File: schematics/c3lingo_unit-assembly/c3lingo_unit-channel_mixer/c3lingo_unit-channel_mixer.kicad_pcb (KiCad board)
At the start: 2 copper layers, 75 x 183 mm, 120 parts, among them J301 Mic X In, J302 Headphone X, J303 PowerSupply, J304 Inputs, J305 Output, J306 PowerSupply, J307 Interconnect, J308 Interconnect, SW301 OnAir_X, SW302 Mute_X, U301 NE5534, U302 LM833N, U303 LM386N-4, U304 LM833N, U305 LM339, U306 LM339, U307 LM339

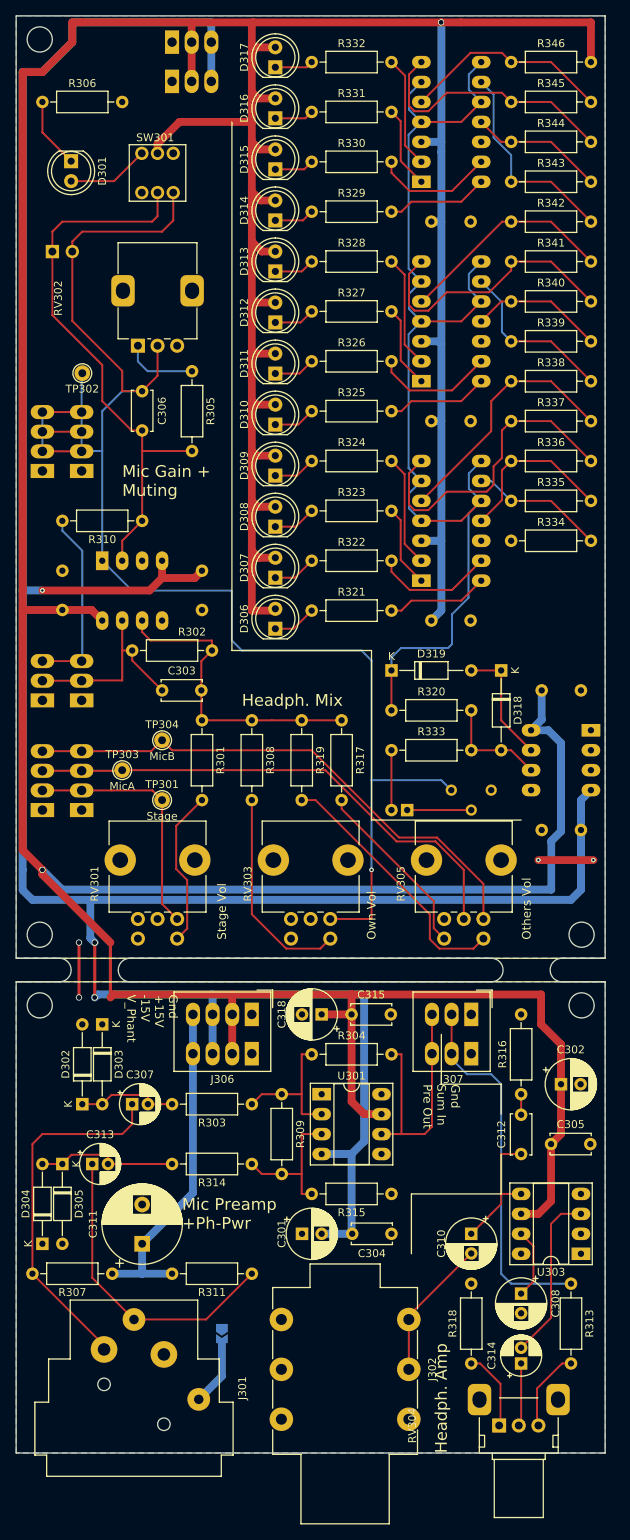
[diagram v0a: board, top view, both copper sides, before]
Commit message: [TIDY] Split channel into two schematics
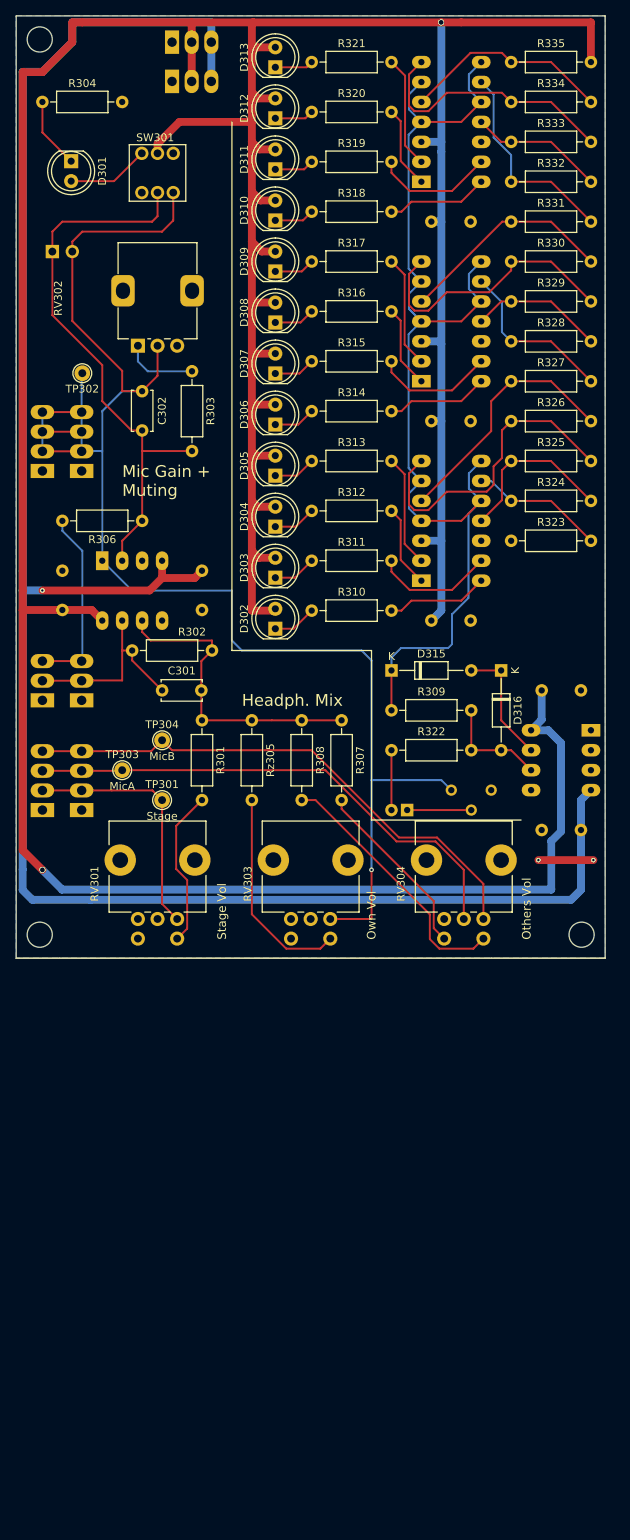
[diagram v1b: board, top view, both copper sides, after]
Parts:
- removed the C301 at (86.4, 205.1)
- removed the C302 at (119.4, 186.0)
- removed the C304 at (97.8, 205.1)
- removed the C305 at (118.1, 193.7)
- removed the C307 at (64.8, 188.6)
- removed the C308 at (114.3, 212.7)
- removed the C310 at (108.0, 205.1)
- removed C311: 100uF/ 63V, Capacitor_THT:CP_Radial_D10.0mm_P5.00mm
- removed C312: 47nF, Capacitor_THT:C_Disc_D5.0mm_W2.5mm_P5.00mm
- removed C313: 1uF/ 63V lowESR, Capacitor_THT:CP_Radial_D5.0mm_P2.00mm
- removed C314: 1uF, Capacitor_THT:CP_Radial_D5.0mm_P2.00mm
- removed C315: 100nF, Capacitor_THT:C_Disc_D5.0mm_W2.5mm_P5.00mm
- removed C318: 100uF, Capacitor_THT:CP_Radial_D6.3mm_P2.50mm
- removed the D302 at (58.4, 188.6)
- removed the D303 at (61.0, 178.4)
- removed the D304 at (53.3, 206.4)
- removed the D305 at (55.9, 196.2)
- removed H305, H306: MountingHole, MountingHole:MountingHole_3.2mm_M3
- removed the J302 at (100.0, 216.0)
- removed J306: PowerSupply, TerminalBlock_Phoenix:TerminalBlock_Phoenix_PTSM-0,5-4-2.5-H-THR_1x04_P2.50mm_Horizontal
- removed J307, J308: Interconnect, TerminalBlock_Phoenix:TerminalBlock_Phoenix_PTSM-0,5-3-2.5-H-THR_1x03_P2.50mm_Horizontal
- removed JP302: GND_JMP, Jumper:SolderJumper-2_P1.3mm_Open_TrianglePad1.0x1.5mm
- removed the R303 at (80.0, 188.6)
- removed the R304 at (87.6, 182.2)
- removed the R307 at (62.2, 210.2)
- removed the R308 at (80.0, 139.7)
- removed the R309 at (83.8, 187.3)
- removed the R310 at (66.0, 114.3)
- removed the R311 at (80.0, 210.2)
- removed the R313 at (120.7, 211.4)
- removed the R314 at (80.0, 196.2)
- removed the R315 at (97.8, 200.0)
- removed the R316 at (114.3, 187.3)
- removed the R318 at (108.0, 221.6)
- removed the RV304 at (111.5, 229.5)
- removed the U301 at (88.9, 187.3)
- removed the U303 at (121.9, 207.6)
- added R306: 330R, Resistor_THT:R_Axial_DIN0207_L6.3mm_D2.5mm_P10.16mm_Horizontal, F.Cu at (66.0, 114.3)
- added Rz305: 22K, Resistor_THT:R_Axial_DIN0207_L6.3mm_D2.5mm_P10.16mm_Horizontal, F.Cu at (80.0, 139.7)
- J301: value Mic X In -> Interconnect; footprint Connector_Audio:Jack_XLR_Neutrik_NC3FAAH2_Horizontal -> TerminalBlock_Phoenix:TerminalBlock_Phoenix_PTSM-0,5-3-2.5-H-THR_1x03_P2.50mm_Horizontal; moved to B.Cu
- moved J301 84.7 mm to (53.3, 137.2), turned to 90 degrees
- renumbered C303 to C301, C306 to C302, C316 to C303, C317 to C304, C319 to C305, C321 to C306, C322 to C307, C323 to C308, C324 to C309, C325 to C310, D306 to D302, D307 to D303, D308 to D304, D309 to D305, D310 to D306, D311 to D307, D312 to D308, D313 to D309, D314 to D310, D315 to D311, D316 to D312, D317 to D313, D319 to D315, D318 to D316, J303 to J302, J305 to J303, R305 to R303, R306 to R304, R317 to R307, R319 to R308, R320 to R309, R321 to R310, R322 to R311, R323 to R312, R324 to R313, R325 to R314, R326 to R315, R327 to R316, R328 to R317, R329 to R318, R330 to R319, R331 to R320, R332 to R321, R333 to R322, R334 to R323, R335 to R324, R336 to R325, R337 to R326, R338 to R327, R339 to R328, R340 to R329, R341 to R330, R342 to R331, R343 to R332, R344 to R333, R345 to R334, R346 to R335, RV305 to RV304, RV306 to RV305, U302 to U301, U305 to U302, U306 to U303, U307 to U304, U304 to U305
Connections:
- C301 pad 1: SumOut -> /HeadphoneMix
- J301 pad 2: Net-(C307-Pad1) -> /HeadphoneMix
- J301 pad 3: Net-(C313-Pad1) -> /MicGainIn
- R302 pad 1: SumOut -> /HeadphoneMix
- U301 pad 7: SumOut -> /HeadphoneMix
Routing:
- net +15V: track 649.8 -> 513.1 mm
- net -15V: track 344.7 -> 251.3 mm, vias 3 -> 1
- net AmpIn: track 46.9 -> 0.00 mm
- net Net-(C307-Pad1): track 46.2 -> 0.00 mm
- net V_Phant: track 43.3 -> 0.00 mm
- net Net-(C313-Pad1): track 39.4 -> 0.00 mm
- net MicPreOut: track 32.7 -> 0.00 mm
- net SumOut: track 25.7 -> 0.00 mm
- net /HeadphoneMix: track 0.00 -> 25.7 mm
- net MicGainIn: track 23.8 -> 0.00 mm
- net /MicGainIn: track 0.00 -> 23.8 mm
- net Net-(C314-Pad2): track 21.7 -> 0.00 mm
- net Net-(R309-Pad2): track 18.3 -> 0.00 mm
- net Net-(R303-Pad1) (its old number): track 18.3 -> 0.00 mm
- net Net-(C313-Pad2): track 18.1 -> 0.00 mm
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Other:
- board size 75 x 183 mm -> 75 x 120 mm
- board text removed: "Gnd +15V -15V V_Phant"
- board text removed: "Gnd Sum In Pre Out"
- board text removed: "Headph. Amp"
- board text removed: "Mic Preamp +Ph-Pwr"
- board text removed: "c3lingo Interpreter Unit v0.3 2023-12-30 Jannik Beyerstedt (jtbx)"

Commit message: Update to KiCad 7
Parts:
- removed D316: 1N4148, Diode_THT:D_DO-35_SOD27_P10.16mm_Horizontal
- removed Rz305: 22K, Resistor_THT:R_Axial_DIN0207_L6.3mm_D2.5mm_P10.16mm_Horizontal
- added D314: 1N4148, Diode_THT:D_DO-35_SOD27_P10.16mm_Horizontal, F.Cu at (111.8, 133.3)
- added R305: 22K, Resistor_THT:R_Axial_DIN0207_L6.3mm_D2.5mm_P10.16mm_Horizontal, F.Cu at (80.0, 139.7)
- C302: value 100nF -> 10nF

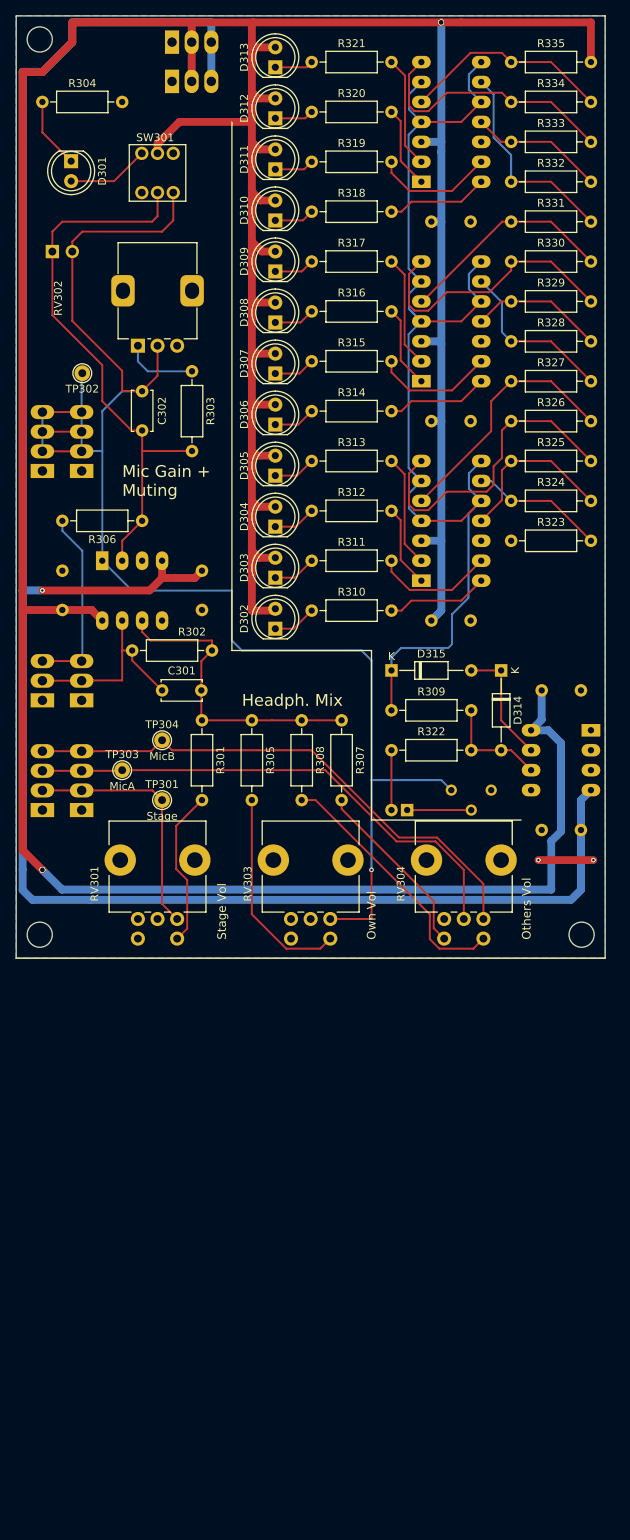
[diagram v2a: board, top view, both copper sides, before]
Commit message: Re-layout boards with SMD components
* Channel Mix: Removed vu meter potentiometer as good setting was found (10 dB
  more headroom)
* Channel Mix: Add vu meter alternate power
* Channel I/O: Added jumper for phantom power enable/disable
* Add GND test points
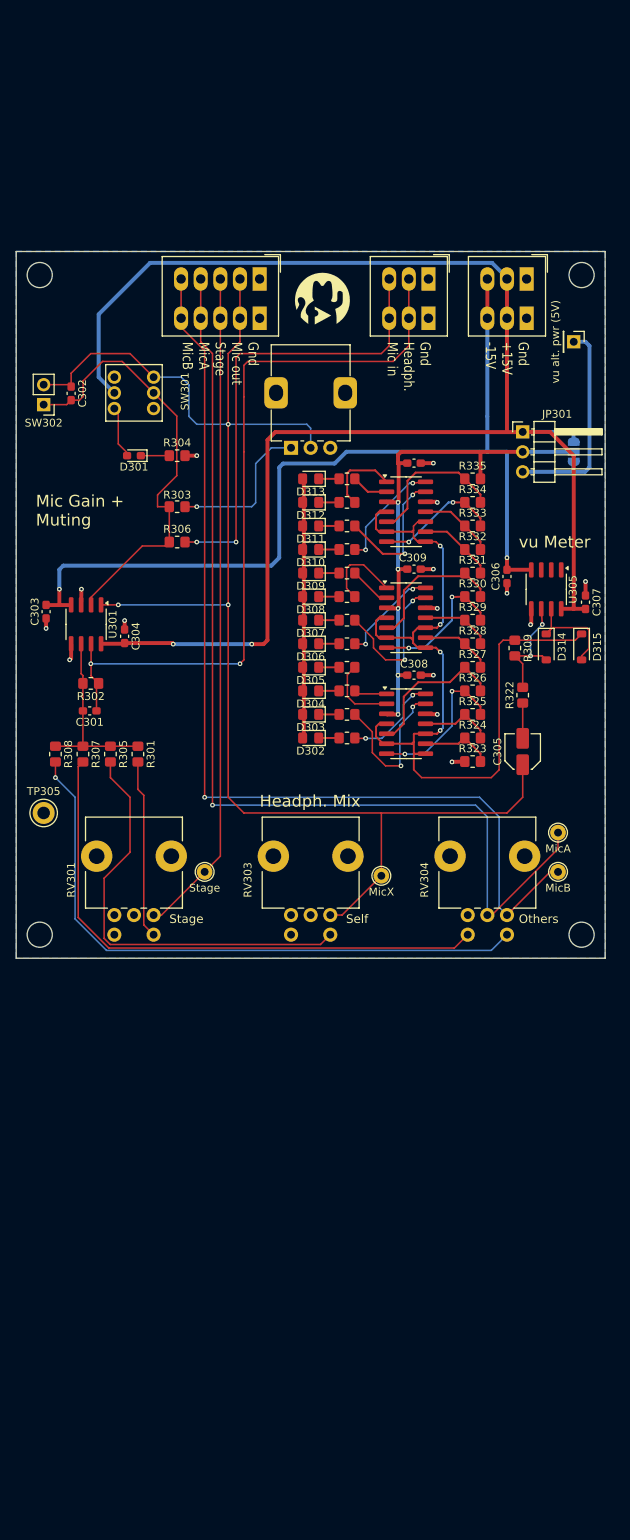
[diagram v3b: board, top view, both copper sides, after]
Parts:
- removed RV305: 50K, Potentiometer_THT:Potentiometer_Vishay_T73XX_Horizontal
- added G***: LOGO, c3lingo_unit-footprints:voctocat-07mm, F.Cu at (89.0, 86.0)
- added G***: LOGO, c3lingo_unit-footprints:voctocat-25mm, B.Cu at (87.5, 121.0)
- added H304: MountingHole, MountingHole:MountingHole_3.2mm_M3, F.Cu at (122.0, 83.0)
- added JP301: vu PWR, Connector_PinHeader_2.54mm:PinHeader_1x03_P2.54mm_Horizontal, F.Cu at (114.5, 103.0)
- added JP302: vu PWR, Jumper:SolderJumper-3_P1.3mm_Open_RoundedPad1.0x1.5mm_NumberLabels, B.Cu at (121.0, 105.5)
- added TP305: GND, TestPoint:TestPoint_Keystone_5005-5009_Compact, F.Cu at (53.5, 151.5)
- C301, C302: footprint Capacitor_THT:C_Disc_D5.0mm_W2.5mm_P5.00mm -> Capacitor_SMD:C_0603_1608Metric_Pad1.08x0.95mm_HandSolder
- C303, C304, C306, C307, C308, C309, C310: footprint Capacitor_THT:C_Disc_D5.0mm_W2.5mm_P5.00mm -> Capacitor_SMD:C_0603_1608Metric_Pad1.08x0.95mm_HandSolder; moved to F.Cu
- C305: footprint Capacitor_THT:CP_Radial_D5.0mm_P2.00mm -> Capacitor_SMD:C_Elec_4x5.8; moved to F.Cu
- D301: footprint LED_THT:LED_D5.0mm -> LED_SMD:LED_0603_1608Metric_Pad1.05x0.95mm_HandSolder
- D302, D303, D304, D305, D306, D307, D308, D309, D310, D311, D312, D313: footprint LED_THT:LED_D5.0mm -> LED_SMD:LED_0805_2012Metric_Pad1.15x1.40mm_HandSolder
- D314, D315: footprint Diode_THT:D_DO-35_SOD27_P10.16mm_Horizontal -> Diode_SMD:D_SOD-123
- J301, J302, SW302: moved to F.Cu
- J303: value Output -> I/O; footprint TerminalBlock_Phoenix:TerminalBlock_Phoenix_PTSM-0,5-4-2.5-H-THR_1x04_P2.50mm_Horizontal -> TerminalBlock_Phoenix:TerminalBlock_Phoenix_PTSM-0,5-5-2.5-H-THR_1x05_P2.50mm_Horizontal; moved to F.Cu
- J304: value Inputs -> vu alt. pwr (5V); footprint TerminalBlock_Phoenix:TerminalBlock_Phoenix_PTSM-0,5-4-2.5-H-THR_1x04_P2.50mm_Horizontal -> Connector_PinHeader_2.54mm:PinHeader_1x01_P2.54mm_Vertical; moved to F.Cu
- R301, R302, R303, R304, R305, R306, R307, R308, R322, R323, R324, R325, R326, R327, R328, R329, R330, R331, R332, R333, R334, R335: footprint Resistor_THT:R_Axial_DIN0207_L6.3mm_D2.5mm_P10.16mm_Horizontal -> Resistor_SMD:R_0805_2012Metric_Pad1.20x1.40mm_HandSolder
- R309: value 15K -> 12K; footprint Resistor_THT:R_Axial_DIN0207_L6.3mm_D2.5mm_P10.16mm_Horizontal -> Resistor_SMD:R_0805_2012Metric_Pad1.20x1.40mm_HandSolder
- R310, R311, R312, R313, R314, R315, R319, R320, R321: value 390R -> 680R; footprint Resistor_THT:R_Axial_DIN0207_L6.3mm_D2.5mm_P10.16mm_Horizontal -> Resistor_SMD:R_0805_2012Metric_Pad1.20x1.40mm_HandSolder
- R316, R317, R318: value 390R -> 620R; footprint Resistor_THT:R_Axial_DIN0207_L6.3mm_D2.5mm_P10.16mm_Horizontal -> Resistor_SMD:R_0805_2012Metric_Pad1.20x1.40mm_HandSolder
- U301, U305: value LM833N -> LM833-N; footprint Package_DIP:DIP-8_W7.62mm_Socket_LongPads -> Package_SO:SOIC-8_3.9x4.9mm_P1.27mm; moved to F.Cu
- U302, U303, U304: footprint Package_DIP:DIP-14_W7.62mm_Socket_LongPads -> Package_SO:SOIC-14_3.9x8.7mm_P1.27mm; moved to F.Cu
- moved J304 90.2 mm to (121.0, 91.5), turned to -90 degrees
- moved TP302 74.5 mm to (96.5, 159.5), turned to 0 degrees
- moved J301 72.8 mm to (102.5, 83.5), turned to 180 degrees
- moved TP303 56.1 mm to (119.0, 154.0)
- moved J302 54.3 mm to (115.0, 83.5), turned to 180 degrees
- moved R335 53.3 mm to (108.1, 109.0)
- moved R321 53.3 mm to (92.1, 109.0)
- moved TP304 53.1 mm to (119.0, 159.0)
- moved D313 52.6 mm to (87.5, 109.0), turned to 180 degrees
- moved R334 51.2 mm to (108.1, 112.0)
- moved R320 49.9 mm to (92.1, 112.0)
- moved R333 49.2 mm to (108.1, 115.0)
- moved D312 49.1 mm to (87.5, 112.0), turned to 180 degrees
- moved R304 48.2 mm to (70.5, 106.0)
- moved R332 47.1 mm to (108.1, 118.0)
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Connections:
- C305 pad 1: Net-(C305-Pad1) -> /PreampOut
- C308 pad 1: +15V -> Net-(D302-A)
- C309 pad 1: +15V -> Net-(D302-A)
- C310 pad 1: +15V -> Net-(D302-A)
- D302 pad 2: +15V -> Net-(D302-A)
- D303 pad 2: +15V -> Net-(D302-A)
- D304 pad 2: +15V -> Net-(D302-A)
- D305 pad 2: +15V -> Net-(D302-A)
- D306 pad 2: +15V -> Net-(D302-A)
- D307 pad 2: +15V -> Net-(D302-A)
- D308 pad 2: +15V -> Net-(D302-A)
- D309 pad 2: +15V -> Net-(D302-A)
- D310 pad 2: +15V -> Net-(D302-A)
- D311 pad 2: +15V -> Net-(D302-A)
- D312 pad 2: +15V -> Net-(D302-A)
- D313 pad 2: +15V -> Net-(D302-A)
- J303 pad 3: /PreampOut -> /Monitor_Stage
- J303 pad 4: /PreampOut -> /Monitor_OthersA
- J304 pad 1: GND -> +5V
- R335 pad 2: +15V -> Net-(D302-A)
- U302 pad 3: +15V -> Net-(D302-A)
- U303 pad 3: +15V -> Net-(D302-A)
- U304 pad 3: +15V -> Net-(D302-A)
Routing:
- net +15V: track 513.1 -> 204.1 mm
- net -15V: track 251.3 -> 117.7 mm, vias 1 -> 2
- net Net-(D302-A): track 0.00 -> 99.6 mm, vias 0 -> 5
- net /HeadphoneMix: track 25.7 -> 96.8 mm, vias 0 -> 2
- net /Monitor_OthersA: track 65.1 -> 130.3 mm, vias 0 -> 1
- net /Monitor_OthersB: track 68.8 -> 127.8 mm, vias 0 -> 1
- net /Monitor_Stage: track 31.7 -> 85.1 mm
- net Net-(R307-Pad2): track 23.0 -> 72.0 mm
- net Net-(R308-Pad2): track 33.3 -> 78.5 mm, vias 0 -> 1
- net /MicGainIn: track 23.8 -> 58.6 mm, vias 0 -> 2
- net Net-(D315-K): track 142.6 -> 109.7 mm, vias 0 -> 4
- net +5V: track 0.00 -> 27.7 mm
- net Net-(R305-Pad2): track 26.9 -> 54.5 mm
- net Net-(U302B-+): track 39.9 -> 19.8 mm, vias 0 -> 2
- net Net-(U304B-+): track 33.2 -> 15.9 mm, vias 0 -> 2
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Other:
- board size 75 x 120 mm -> 75 x 90 mm
- board text added: "Gnd +15V -15V"
- board text added: "Gnd Headph. Mic in"
- board text added: "Gnd Mic out Stage MicA MicB"
- board text added: "Others"
- board text added: "Self"
- board text added: "Stage"
- board text added: "c3lingo Interpreter Unit Channel Mixer v0.3 2024-07-06"
- board text added: "vu Meter"
- board text removed: "Gnd +15V -15V V_LED"
- board text removed: "Gnd Mic X (3x)"
- board text removed: "Gnd Stage Mic A Mic B"
- board text removed: "Gnd Sum Out Mic In"
- board text removed: "Others Vol"
- board text removed: "Own Vol"
- board text removed: "Stage Vol"
- board text removed: "c3lingo Interpreter Unit v0.3 2022-12-30 Jannik Beyerstedt (jtbx)"
